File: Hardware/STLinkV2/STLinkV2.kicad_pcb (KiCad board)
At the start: 2 copper layers, 73.7 x 38.1 mm, 62 parts, among them J1 USB_B_Micro, J2 SWD, J3 ISP, J4 RS232, J5 JTAG, U1 STM32F103CBT6, U2 SRV05-4, U3 HT7833, U4 SRV05-4, U5 SRV05-4, U6 74AVCH2T45DC,125, U7 74AVCH2T45DC,125, Y1 8MHz

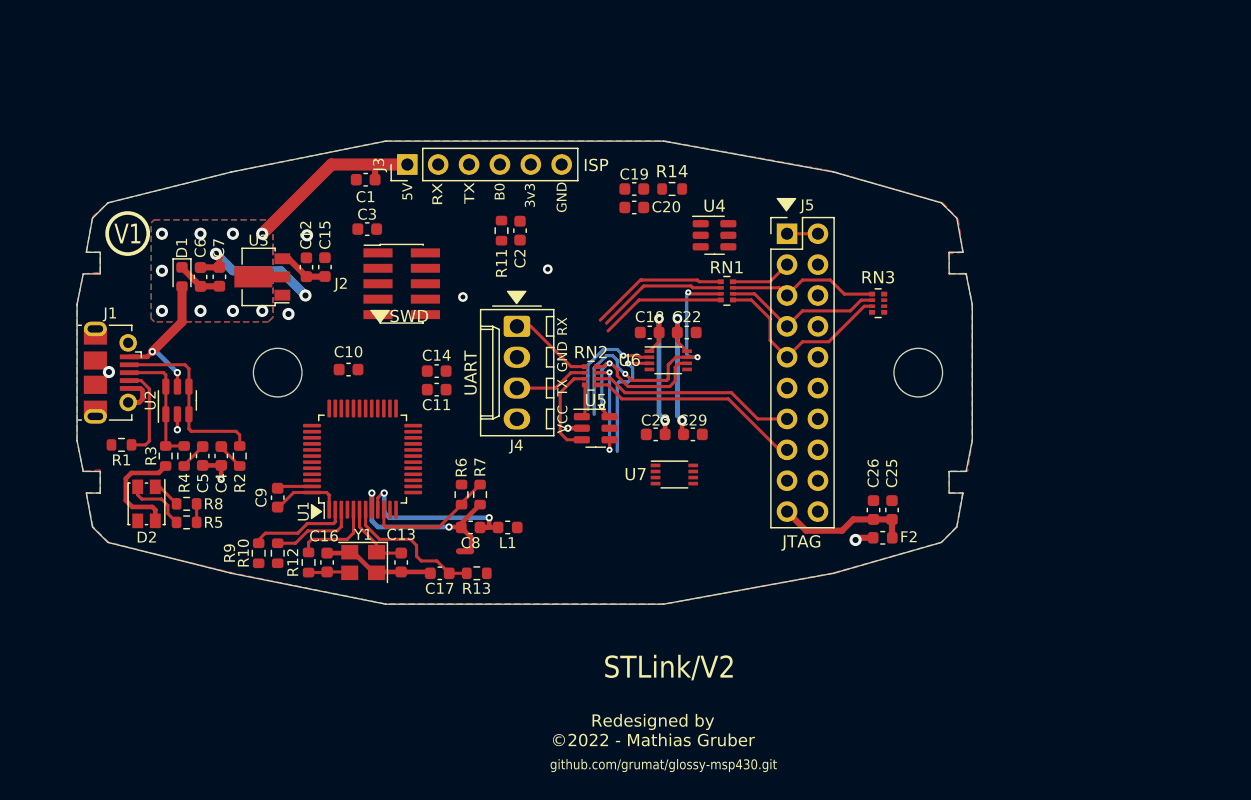
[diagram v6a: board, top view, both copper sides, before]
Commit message: STLink V2 hardware review
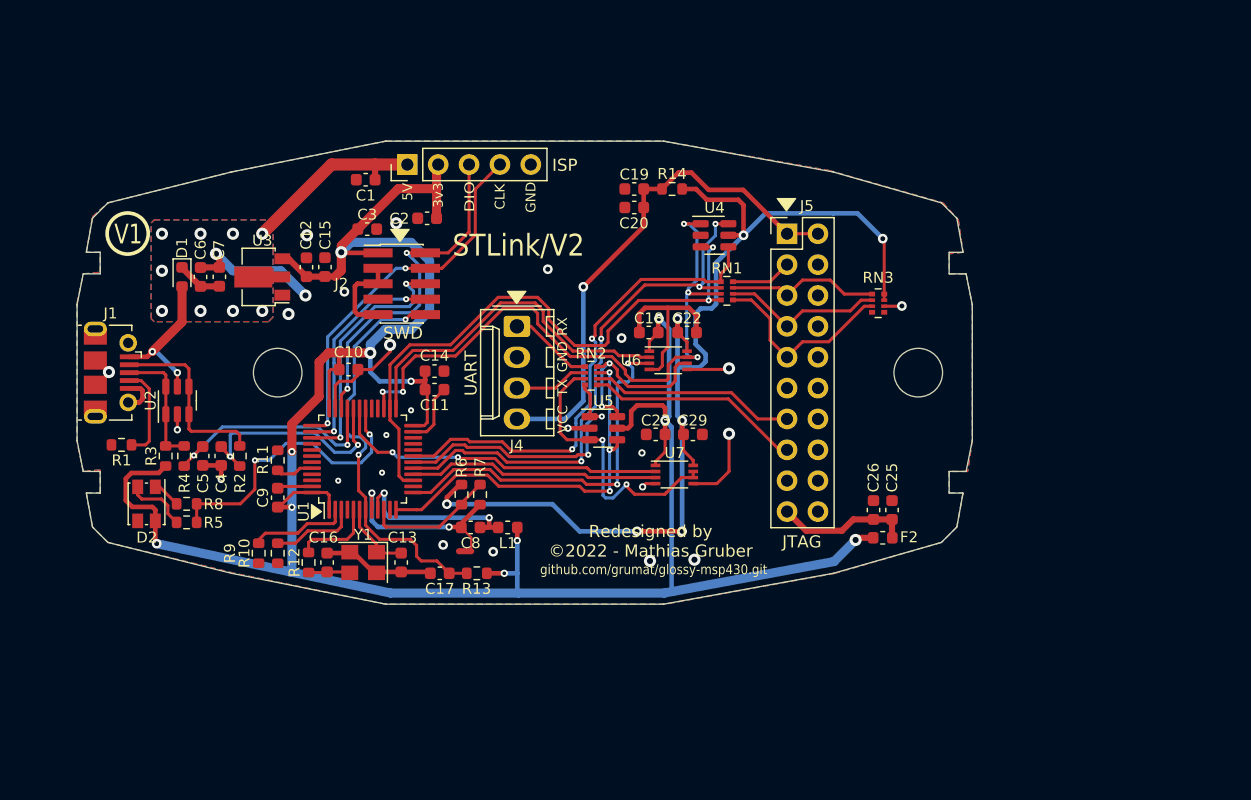
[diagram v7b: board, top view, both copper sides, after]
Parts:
- J3: footprint Connector_PinHeader_2.54mm:PinHeader_1x06_P2.54mm_Vertical -> Connector_PinHeader_2.54mm:PinHeader_1x05_P2.54mm_Vertical
- moved R11 26.4 mm to (80.0, 77.1), turned to -90 degrees
- moved C2 7.71 mm to (92.3, 57.1), turned to 180 degrees
- moved U5 0.64 mm to (106.8, 74.4)
- moved C11 0.18 mm to (92.9, 71.2)
- moved C14 0.18 mm to (92.9, 69.7)
- moved C18 0.08 mm to (110.5, 66.5)
- turned C19 to 180 degrees
- turned C20 to 180 degrees
- turned C3 to 0 degrees
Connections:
- J3 pad 2: /SWO -> +3V3
- J3 pad 3: /LED -> /STM_TMS
- J3 pad 4: /BOOT0 -> /STM_TCK
- J3 pad 5: +3V3 -> GND
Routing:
- net +3V3: track 33.6 -> 207.7 mm, vias 3 -> 11
- net VCC: track 12.8 -> 90.1 mm, vias 2 -> 7
- net GND: track 32.0 -> 80.5 mm, vias 10 -> 26
- net /T_VCC: track 2.54 -> 42.6 mm, vias 0 -> 1
- net /TCK_SWCLK: track 10.3 -> 50.1 mm, vias 0 -> 2
- net /TDI: track 10.7 -> 44.7 mm, vias 0 -> 4
- net /STM_TCK: track 0.00 -> 30.7 mm, vias 0 -> 2
- net /TRST: track 11.3 -> 40.5 mm, vias 0 -> 2
- net /STM_TMS: track 0.00 -> 28.9 mm, vias 0 -> 2
- net /TMS_SWDIO: track 24.2 -> 52.7 mm, vias 3 -> 5
- net /SWO: track 0.00 -> 27.7 mm, vias 0 -> 2
- net /TTXD: track 8.24 -> 31.4 mm, vias 2 -> 3
- net /LED: track 1.52 -> 24.2 mm, vias 0 -> 2
- net /STM_NRST: track 11.8 -> 33.9 mm, vias 0 -> 2
- net /STM_TDO: track 0.00 -> 21.0 mm, vias 0 -> 2
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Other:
- board text added: "CLK"
- board text added: "DIO"
- board text removed: "B0"

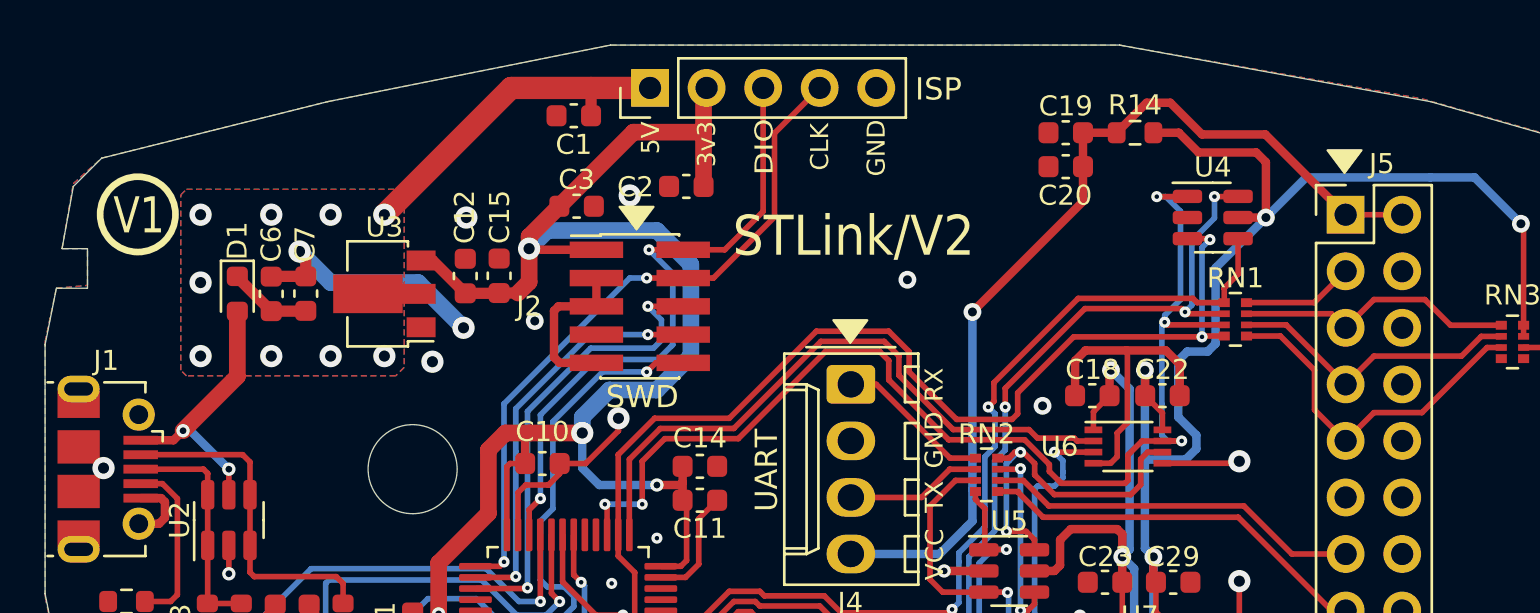
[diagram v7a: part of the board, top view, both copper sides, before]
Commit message: Minor tweaks on VCC (ref)
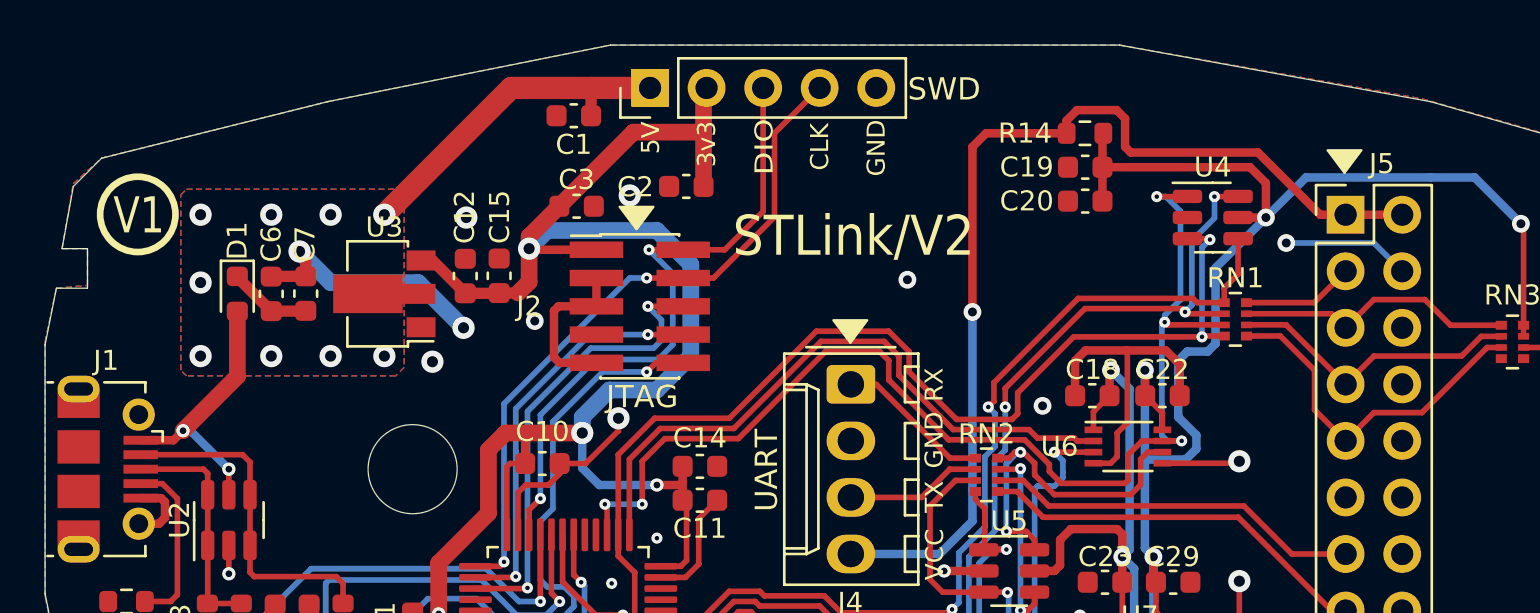
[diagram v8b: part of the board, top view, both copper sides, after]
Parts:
- RN1, RN2: value 22 -> 47
- moved R14 2.25 mm to (110.2, 54.8)
- moved C19 1.78 mm to (110.2, 56.3)
- moved C20 1.78 mm to (110.2, 57.8)
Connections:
- C19 pad 1: /T_VCC -> VCC
- C20 pad 1: /T_VCC -> VCC
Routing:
- net GND: track 80.5 -> 86.2 mm
- net VCC: track 90.1 -> 94.3 mm
- net /T_VCC: track 42.6 -> 45.9 mm
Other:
- board text removed: "ISP"
